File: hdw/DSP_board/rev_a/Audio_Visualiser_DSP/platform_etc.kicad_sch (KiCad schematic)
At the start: 10 parts, among them U1001 DS1683, U1002 MCP9804

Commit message: assigned many digi-key part numbers
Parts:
- C1001, C1002, C1003: Digi-Key PN (none) -> 1276-CL05A106MP6NUN8CT-ND
- C1004, C1005: Digi-Key PN (none) -> 1276-CL05B104KB5NNNCCT-ND
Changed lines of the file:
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@@
 			)
 		)
-		(property "Digi-Key PN" ""
+		(property "Digi-Key PN" "1276-CL05A106MP6NUN8CT-ND"
 			(at 69.215 59.69 0)
 			(hide yes)
@@
 			)
 		)
-		(property "Digi-Key PN" ""
+		(property "Digi-Key PN" "1276-CL05A106MP6NUN8CT-ND"
 			(at 102.235 59.69 0)
 			(hide yes)
@@
 			)
 		)
-		(property "Digi-Key PN" ""
+		(property "Digi-Key PN" "1276-CL05B104KB5NNNCCT-ND"
 			(at 173.99 113.03 0)
 			(hide yes)
@@
 			)
 		)
-		(property "Digi-Key PN" ""
+		(property "Digi-Key PN" "1276-CL05B104KB5NNNCCT-ND"
 			(at 107.95 72.39 0)
 			(hide yes)
@@
 			)
 		)
-		(property "Digi-Key PN" ""
+		(property "Digi-Key PN" "1276-CL05A106MP6NUN8CT-ND"
 			(at 85.725 59.69 0)
 			(hide yes)

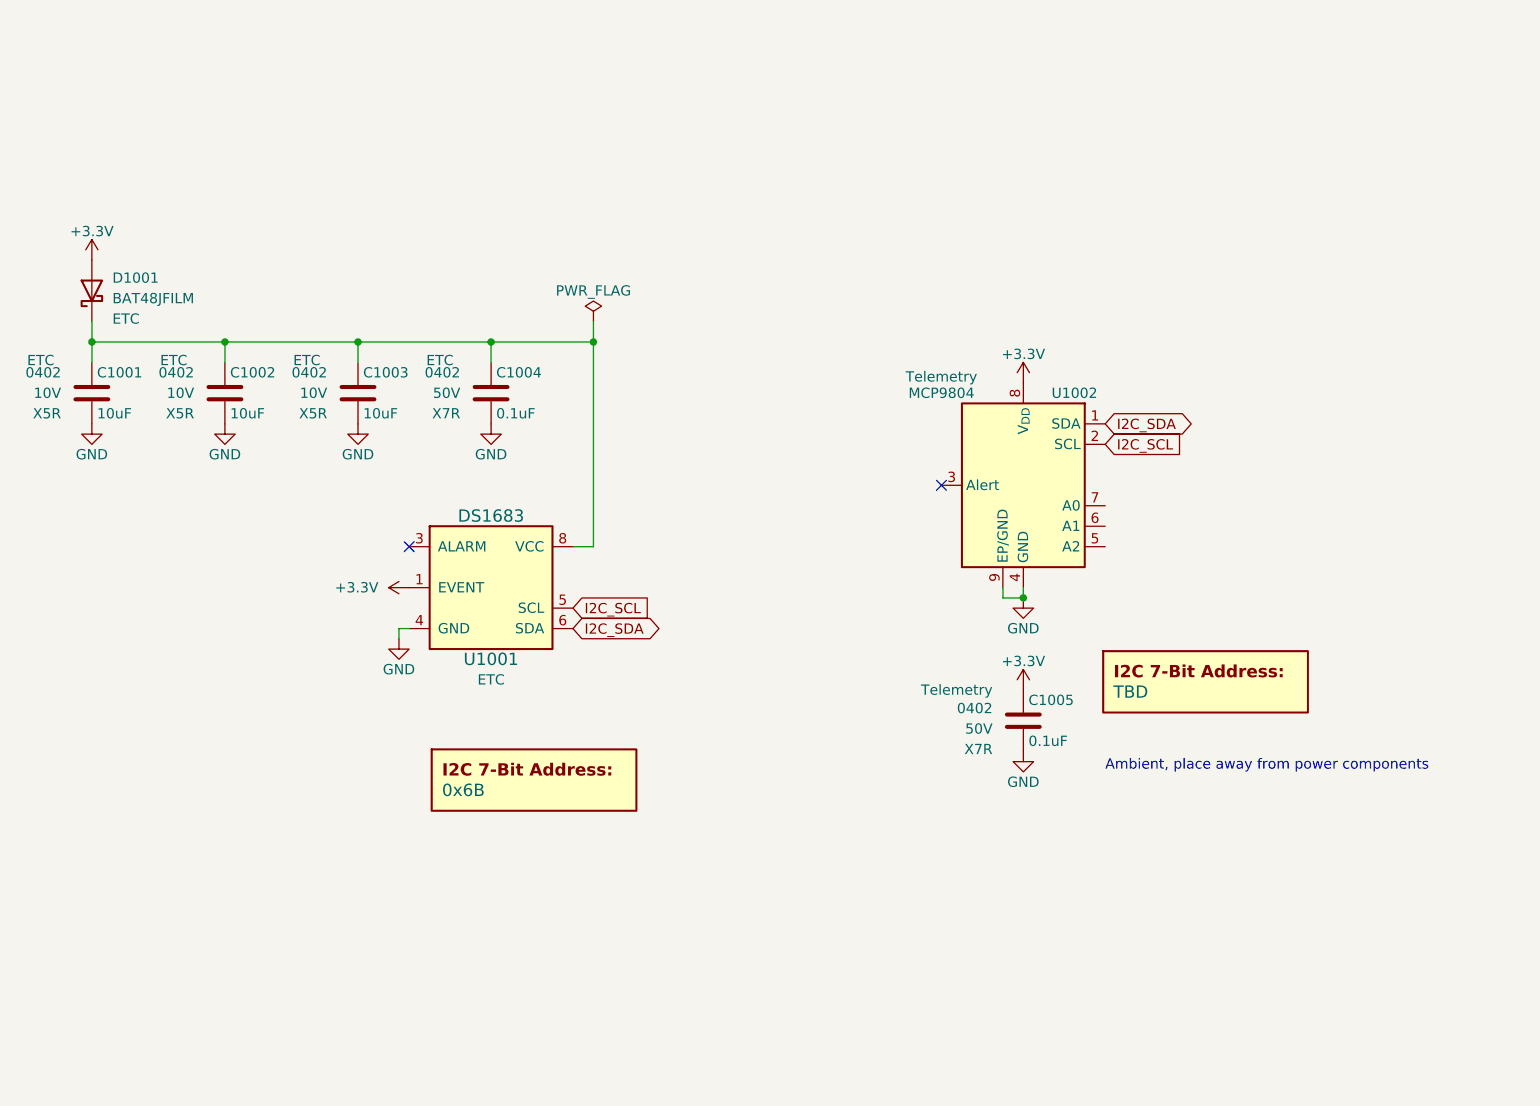
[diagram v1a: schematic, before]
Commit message: Added a bunch of stuff to the schematic
Moved to adafruit I2C rotary encoder module. Added signal test points. Added some design schematic notes. Added LEd output connector ESD diodes. Consolidated on a single schottky diode. Connected most signals to MCU
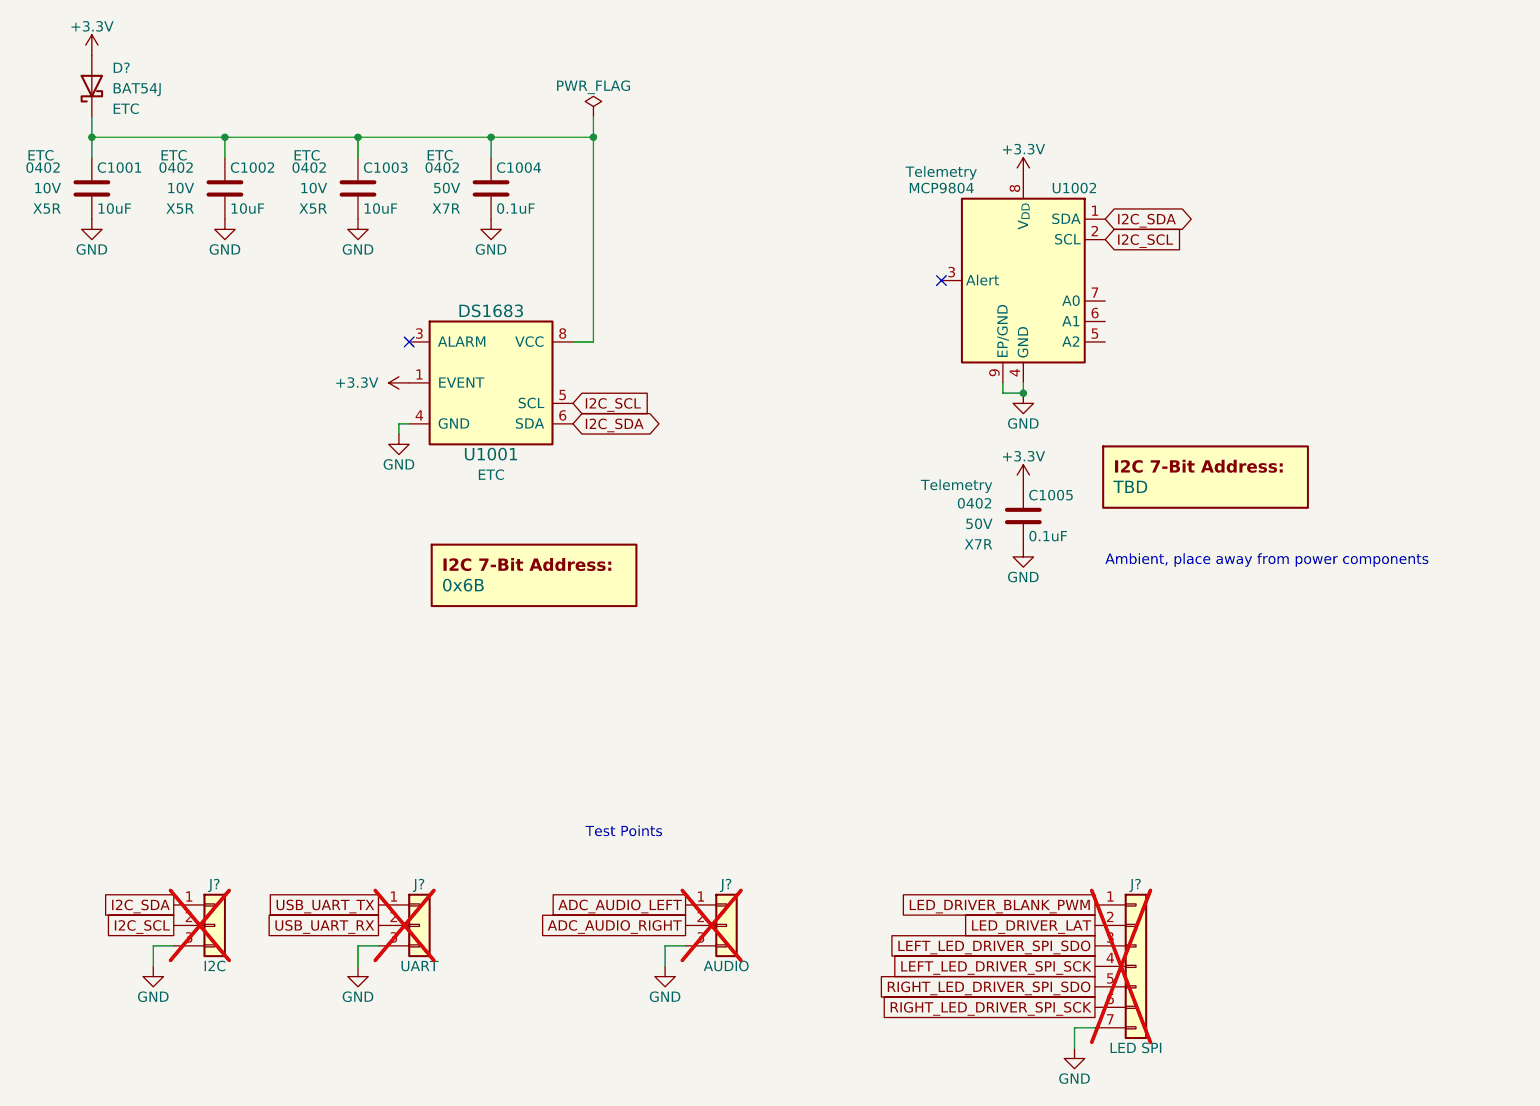
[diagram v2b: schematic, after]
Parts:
- removed D1001: BAT48JFILM, Diode_SMD:D_SOD-323, symbol Diode:BAT48JFILM
- added D?: BAT54J, Diode_SMD:D_SOD-323F, symbol Diode:BAT54J
- added J?: AUDIO, symbol Connector_Generic:Conn_01x03
- added J?: UART, symbol Connector_Generic:Conn_01x03
- added J?: LED SPI, symbol Connector_Generic:Conn_01x07
- added J?: I2C, symbol Connector_Generic:Conn_01x03
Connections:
- net +3.3V: now also D?.2 (A)
- net GND: now also J?.3 (Pin_3), J?.3 (Pin_3), J?.3 (Pin_3), J?.7 (Pin_7)
- net I2C_SCL: now also J?.2 (Pin_2)
- net I2C_SDA: now also J?.1 (Pin_1)
- net at C1001.1, C1002.1, C1003.1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: now also D?.1 (K)
- new net ADC_AUDIO_LEFT: J?.1 (Pin_1)
- new net ADC_AUDIO_RIGHT: J?.2 (Pin_2)
- new net LED_DRIVER_BLANK_PWM: J?.1 (Pin_1)
- new net LED_DRIVER_LAT: J?.2 (Pin_2)
- new net LEFT_LED_DRIVER_SPI_SCK: J?.4 (Pin_4)
- new net LEFT_LED_DRIVER_SPI_SDO: J?.3 (Pin_3)
- new net RIGHT_LED_DRIVER_SPI_SCK: J?.6 (Pin_6)
- new net RIGHT_LED_DRIVER_SPI_SDO: J?.5 (Pin_5)
- new net USB_UART_RX: J?.2 (Pin_2)
- new net USB_UART_TX: J?.1 (Pin_1)
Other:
- note added: "Test Points"
- moved on the sheet: C1001, C1002, C1003, C1004, C1005, U1001, U1002

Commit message: Added simulation outputs, sim readme
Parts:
- gave numbers to parts that had none: 5
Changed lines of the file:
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@@
 		(in_pos_files yes)
 		(dnp yes)
-		(property "Reference" "J?"
+		(property "Reference" "J1003"
 			(at 137.16 133.35 0)
 			(show_name no)
@@
 			(project "Audio_Visualiser_DSP"
 				(path "/97a4dfb8-0e16-46f1-9709-8d2007dd0cd3/546058cd-0694-4b2f-adfe-f6c0887c2b7f"
-					(reference "J?")
+					(reference "J1003")
 					(unit 1)
 				)
@@
 		(in_pos_files yes)
 		(dnp no)
-		(property "Reference" "#PWR01003"
+		(property "Reference" "#PWR01004"
 			(at 74.93 57.15 0)
 			(hide yes)
@@
 			(project "Audio_Visualiser_DSP"
 				(path "/97a4dfb8-0e16-46f1-9709-8d2007dd0cd3/546058cd-0694-4b2f-adfe-f6c0887c2b7f"
-					(reference "#PWR01003")
+					(reference "#PWR01004")
 					(unit 1)
 				)
@@
 		(in_pos_files yes)
 		(dnp yes)
-		(property "Reference" "J?"
+		(property "Reference" "J1002"
 			(at 99.06 133.35 0)
 			(show_name no)
@@
 			(project "Audio_Visualiser_DSP"
 				(path "/97a4dfb8-0e16-46f1-9709-8d2007dd0cd3/546058cd-0694-4b2f-adfe-f6c0887c2b7f"
-					(reference "J?")
+					(reference "J1002")
 					(unit 1)
 				)
@@
 		(in_pos_files yes)
 		(dnp yes)
-		(property "Reference" "J?"
+		(property "Reference" "J1004"
 			(at 187.96 133.35 0)
 			(show_name no)
@@
 			(project "Audio_Visualiser_DSP"
 				(path "/97a4dfb8-0e16-46f1-9709-8d2007dd0cd3/546058cd-0694-4b2f-adfe-f6c0887c2b7f"
-					(reference "J?")
+					(reference "J1004")
 					(unit 1)
 				)
@@
 		(in_pos_files yes)
 		(dnp no)
-		(property "Reference" "#PWR01014"
+		(property "Reference" "#PWR01010"
 			(at 129.54 149.86 0)
 			(hide yes)
@@
 			(project "Audio_Visualiser_DSP"
 				(path "/97a4dfb8-0e16-46f1-9709-8d2007dd0cd3/546058cd-0694-4b2f-adfe-f6c0887c2b7f"
-					(reference "#PWR01014")
+					(reference "#PWR01010")
 					(unit 1)
 				)
@@
 		(in_pos_files yes)
 		(dnp no)
-		(property "Reference" "#PWR01011"
+		(property "Reference" "#PWR01014"
 			(at 173.99 97.79 0)
 			(hide yes)
@@
 			(project "Audio_Visualiser_DSP"
 				(path "/97a4dfb8-0e16-46f1-9709-8d2007dd0cd3/546058cd-0694-4b2f-adfe-f6c0887c2b7f"
-					(reference "#PWR01011")
+					(reference "#PWR01014")
 					(unit 1)
 				)
@@
 		(in_pos_files yes)
 		(dnp no)
-		(property "Reference" "#PWR01008"
+		(property "Reference" "#PWR01011"
 			(at 173.99 49.53 0)
 			(hide yes)
@@
 			(project "Audio_Visualiser_DSP"
 				(path "/97a4dfb8-0e16-46f1-9709-8d2007dd0cd3/546058cd-0694-4b2f-adfe-f6c0887c2b7f"
-					(reference "#PWR01008")
+					(reference "#PWR01011")
 					(unit 1)
 				)
@@
 		(in_pos_files yes)
 		(dnp no)
-		(property "Reference" "#PWR01012"
+		(property "Reference" "#PWR01003"
 			(at 66.04 149.86 0)
 			(hide yes)
@@
 			(project "Audio_Visualiser_DSP"
 				(path "/97a4dfb8-0e16-46f1-9709-8d2007dd0cd3/546058cd-0694-4b2f-adfe-f6c0887c2b7f"
-					(reference "#PWR01012")
+					(reference "#PWR01003")
 					(unit 1)
 				)
@@
 		(dnp no)
 		(fields_autoplaced yes)
-		(property "Reference" "#PWR01006"
+		(property "Reference" "#PWR01008"
 			(at 101.6 71.12 0)
 			(hide yes)
@@
 			(project "Audio_Visualiser_DSP"
 				(path "/97a4dfb8-0e16-46f1-9709-8d2007dd0cd3/546058cd-0694-4b2f-adfe-f6c0887c2b7f"
-					(reference "#PWR01006")
+					(reference "#PWR01008")
 					(unit 1)
 				)
@@
 		(dnp no)
 		(fields_autoplaced yes)
-		(property "Reference" "D?"
+		(property "Reference" "D1001"
 			(at 60.96 32.0674 90)
 			(show_name no)
@@
 			(project "Audio_Visualiser_DSP"
 				(path "/97a4dfb8-0e16-46f1-9709-8d2007dd0cd3/546058cd-0694-4b2f-adfe-f6c0887c2b7f"
-					(reference "D?")
+					(reference "D1001")
 					(unit 1)
 				)
@@
 		(in_pos_files yes)
 		(dnp no)
-		(property "Reference" "#PWR01009"
+		(property "Reference" "#PWR01012"
 			(at 173.99 78.74 0)
 			(hide yes)
@@
 			(project "Audio_Visualiser_DSP"
 				(path "/97a4dfb8-0e16-46f1-9709-8d2007dd0cd3/546058cd-0694-4b2f-adfe-f6c0887c2b7f"
-					(reference "#PWR01009")
+					(reference "#PWR01012")
 					(unit 1)
 				)
@@
 		(in_pos_files yes)
 		(dnp yes)
-		(property "Reference" "J?"
+		(property "Reference" "J1001"
 			(at 73.66 133.35 0)
 			(show_name no)
@@
 			(project "Audio_Visualiser_DSP"
 				(path "/97a4dfb8-0e16-46f1-9709-8d2007dd0cd3/546058cd-0694-4b2f-adfe-f6c0887c2b7f"
-					(reference "J?")
+					(reference "J1001")
 					(unit 1)
 				)
@@
 		(in_pos_files yes)
 		(dnp no)
-		(property "Reference" "#PWR01010"
+		(property "Reference" "#PWR01013"
 			(at 173.99 87.63 0)
 			(hide yes)
@@
 			(project "Audio_Visualiser_DSP"
 				(path "/97a4dfb8-0e16-46f1-9709-8d2007dd0cd3/546058cd-0694-4b2f-adfe-f6c0887c2b7f"
-					(reference "#PWR01010")
+					(reference "#PWR01013")
 					(unit 1)
 				)
@@
 		(in_pos_files yes)
 		(dnp no)
-		(property "Reference" "#PWR01004"
+		(property "Reference" "#PWR01005"
 			(at 91.44 57.15 0)
 			(hide yes)
@@
 			(project "Audio_Visualiser_DSP"
 				(path "/97a4dfb8-0e16-46f1-9709-8d2007dd0cd3/546058cd-0694-4b2f-adfe-f6c0887c2b7f"
-					(reference "#PWR01004")
+					(reference "#PWR01005")
 					(unit 1)
 				)
@@
 		(in_pos_files yes)
 		(dnp no)
-		(property "Reference" "#PWR01013"
+		(property "Reference" "#PWR01006"
 			(at 91.44 149.86 0)
 			(hide yes)
@@
 			(project "Audio_Visualiser_DSP"
 				(path "/97a4dfb8-0e16-46f1-9709-8d2007dd0cd3/546058cd-0694-4b2f-adfe-f6c0887c2b7f"
-					(reference "#PWR01013")
+					(reference "#PWR01006")
 					(unit 1)
 				)
@@
 		(in_pos_files yes)
 		(dnp no)
-		(property "Reference" "#PWR01005"
+		(property "Reference" "#PWR01007"
 			(at 96.52 83.82 0)
 			(hide yes)
@@
 			(project "Audio_Visualiser_DSP"
 				(path "/97a4dfb8-0e16-46f1-9709-8d2007dd0cd3/546058cd-0694-4b2f-adfe-f6c0887c2b7f"
-					(reference "#PWR01005")
+					(reference "#PWR01007")
 					(unit 1)
 				)
@@
 		(in_pos_files yes)
 		(dnp no)
-		(property "Reference" "#PWR01007"
+		(property "Reference" "#PWR01009"
 			(at 107.95 57.15 0)
 			(hide yes)
@@
 			(project "Audio_Visualiser_DSP"
 				(path "/97a4dfb8-0e16-46f1-9709-8d2007dd0cd3/546058cd-0694-4b2f-adfe-f6c0887c2b7f"
-					(reference "#PWR01007")
-					(unit 1)
-				)
+					(reference "#PWR01009")
+					(unit 1)
+				)

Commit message: Defined legit KiCad BOM variants
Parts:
- C1001, C1002, C1003, C1004, C1005, D1001, U1001, U1002: now not fitted
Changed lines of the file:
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@@
 		(on_board yes)
 		(in_pos_files yes)
-		(dnp no)
+		(dnp yes)
 		(property "Reference" "C1001"
 			(at 59.055 44.45 0)
@@
 					(reference "C1001")
 					(unit 1)
+					(variant
+						(name "Default")
+					)
+					(variant
+						(name "Development")
+						(dnp no)
+					)
 				)
 			)
@@
 		(on_board yes)
 		(in_pos_files yes)
-		(dnp no)
+		(dnp yes)
 		(property "Reference" "C1003"
 			(at 92.075 44.45 0)
@@
 					(reference "C1003")
 					(unit 1)
+					(variant
+						(name "Default")
+					)
+					(variant
+						(name "Development")
+						(dnp no)
+					)
 				)
 			)
@@
 		(on_board yes)
 		(in_pos_files yes)
-		(dnp no)
+		(dnp yes)
 		(property "Reference" "#PWR01002"
 			(at 58.42 57.15 0)
@@
 					(reference "J1003")
 					(unit 1)
+					(variant
+						(name "Default")
+					)
+					(variant
+						(name "Development")
+					)
 				)
 			)
@@
 		(on_board yes)
 		(in_pos_files yes)
-		(dnp no)
+		(dnp yes)
 		(property "Reference" "U1002"
 			(at 180.34 46.99 0)
@@
 					(reference "U1002")
 					(unit 1)
+					(variant
+						(name "Default")
+					)
+					(variant
+						(name "Development")
+						(dnp no)
+					)
 				)
 			)
@@
 		(on_board yes)
 		(in_pos_files yes)
-		(dnp no)
+		(dnp yes)
 		(property "Reference" "#PWR01004"
 			(at 74.93 57.15 0)
@@
 					(reference "J1002")
 					(unit 1)
+					(variant
+						(name "Default")
+					)
+					(variant
+						(name "Development")
+					)
 				)
 			)
@@
 					(reference "J1004")
 					(unit 1)
+					(variant
+						(name "Default")
+					)
+					(variant
+						(name "Development")
+					)
 				)
 			)
@@
 		(on_board yes)
 		(in_pos_files yes)
-		(dnp no)
+		(dnp yes)
 		(property "Reference" "#PWR01014"
 			(at 173.99 97.79 0)
@@
 					(reference "DOC1001")
 					(unit 1)
+					(variant
+						(name "Default")
+					)
+					(variant
+						(name "Development")
+					)
 				)
 			)
@@
 		(on_board yes)
 		(in_pos_files yes)
-		(dnp no)
+		(dnp yes)
 		(property "Reference" "#PWR01011"
 			(at 173.99 49.53 0)
@@
 					(reference "DOC1002")
 					(unit 1)
+					(variant
+						(name "Default")
+					)
+					(variant
+						(name "Development")
+					)
 				)
 			)
@@
 		(on_board yes)
 		(in_pos_files yes)
-		(dnp no)
+		(dnp yes)
 		(property "Reference" "U1001"
 			(at 107.95 80.01 0)
@@
 					(reference "U1001")
 					(unit 1)
+					(variant
+						(name "Default")
+					)
+					(variant
+						(name "Development")
+						(dnp no)
+					)
 				)
 			)
@@
 		(on_board yes)
 		(in_pos_files yes)
-		(dnp no)
+		(dnp yes)
 		(property "Reference" "C1005"
 			(at 174.625 85.09 0)
@@
 					(reference "C1005")
 					(unit 1)
+					(variant
+						(name "Default")
+					)
+					(variant
+						(name "Development")
+						(dnp no)
+					)
 				)
 			)
@@
 		(on_board yes)
 		(in_pos_files yes)
-		(dnp no)
+		(dnp yes)
 		(fields_autoplaced yes)
 		(property "Reference" "#PWR01008"
@@
 		(on_board yes)
 		(in_pos_files yes)
-		(dnp no)
+		(dnp yes)
 		(fields_autoplaced yes)
 		(property "Reference" "D1001"
@@
 					(reference "D1001")
 					(unit 1)
+					(variant
+						(name "Default")
+					)
+					(variant
+						(name "Development")
+						(dnp no)
+					)
 				)
 			)
@@
 		(on_board yes)
 		(in_pos_files yes)
-		(dnp no)
+		(dnp yes)
 		(property "Reference" "#PWR01012"
 			(at 173.99 78.74 0)
@@
 		(on_board yes)
 		(in_pos_files yes)
-		(dnp no)
+		(dnp yes)
 		(property "Reference" "C1004"
 			(at 108.585 44.45 0)
@@
 					(reference "C1004")
 					(unit 1)
+					(variant
+						(name "Default")
+					)
+					(variant
+						(name "Development")
+						(dnp no)
+					)
 				)
 			)
@@
 					(reference "J1001")
 					(unit 1)
+					(variant
+						(name "Default")
+					)
+					(variant
+						(name "Development")
+					)
 				)
 			)
@@
 		(on_board yes)
 		(in_pos_files yes)
-		(dnp no)
+		(dnp yes)
 		(property "Reference" "#PWR01013"
 			(at 173.99 87.63 0)
@@
 		(on_board yes)
 		(in_pos_files yes)
-		(dnp no)
+		(dnp yes)
 		(property "Reference" "#PWR01005"
 			(at 91.44 57.15 0)
@@
 		(on_board yes)
 		(in_pos_files yes)
-		(dnp no)
+		(dnp yes)
 		(property "Reference" "C1002"
 			(at 75.565 44.45 0)
@@
 					(reference "C1002")
 					(unit 1)
+					(variant
+						(name "Default")
+					)
+					(variant
+						(name "Development")
+						(dnp no)
+					)
 				)
 			)
@@
 		(on_board yes)
 		(in_pos_files yes)
-		(dnp no)
+		(dnp yes)
 		(property "Reference" "#PWR01001"
 			(at 58.42 34.29 0)
@@
 		(on_board yes)
 		(in_pos_files yes)
-		(dnp no)
+		(dnp yes)
 		(property "Reference" "#PWR01007"
 			(at 96.52 83.82 0)
@@
 		(on_board yes)
 		(in_pos_files yes)
-		(dnp no)
+		(dnp yes)
 		(property "Reference" "#FLG01001"
 			(at 120.65 36.195 0)
@@
 		(on_board yes)
 		(in_pos_files yes)
-		(dnp no)
+		(dnp yes)
 		(property "Reference" "#PWR01009"
 			(at 107.95 57.15 0)

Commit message: add new digikey pns
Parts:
- D1001: value BAT54J -> BAT43WS; Digi-Key PN (none) -> BAT43WSRRGCT-ND
- J1001, J1002, J1003: footprint (none) -> Connector_PinSocket_2.54mm:PinSocket_1x03_P2.54mm_Vertical
- J1004: footprint (none) -> Connector_PinSocket_2.54mm:PinSocket_1x07_P2.54mm_Vertical
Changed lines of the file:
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@@
 			)
 		)
-		(property "Footprint" ""
+		(property "Footprint" "Connector_PinSocket_2.54mm:PinSocket_1x03_P2.54mm_Vertical"
 			(at 137.16 138.43 0)
 			(hide yes)
@@
 			)
 		)
-		(property "Footprint" ""
+		(property "Footprint" "Connector_PinSocket_2.54mm:PinSocket_1x03_P2.54mm_Vertical"
 			(at 99.06 138.43 0)
 			(hide yes)
@@
 			)
 		)
-		(property "Footprint" ""
+		(property "Footprint" "Connector_PinSocket_2.54mm:PinSocket_1x07_P2.54mm_Vertical"
 			(at 187.96 143.51 0)
 			(hide yes)
@@
 			)
 		)
-		(property "Value" "BAT54J"
+		(property "Value" "BAT43WS"
 			(at 60.96 34.6074 90)
 			(show_name no)
@@
 				)
 				(justify right)
+			)
+		)
+		(property "Digi-Key PN" "BAT43WSRRGCT-ND"
+			(at 58.42 34.29 0)
+			(hide yes)
+			(show_name no)
+			(do_not_autoplace no)
+			(effects
+				(font
+					(size 1.27 1.27)
+				)
 			)
 		)
@@
 			)
 		)
-		(property "Footprint" ""
+		(property "Footprint" "Connector_PinSocket_2.54mm:PinSocket_1x03_P2.54mm_Vertical"
 			(at 73.66 138.43 0)
 			(hide yes)
